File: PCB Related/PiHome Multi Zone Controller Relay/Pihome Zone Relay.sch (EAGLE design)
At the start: 17 parts, among them IC1 REG1117, M1 WIRELESS-NRF24L01, M3 ARDUINO-PRO-MINI-5.0V

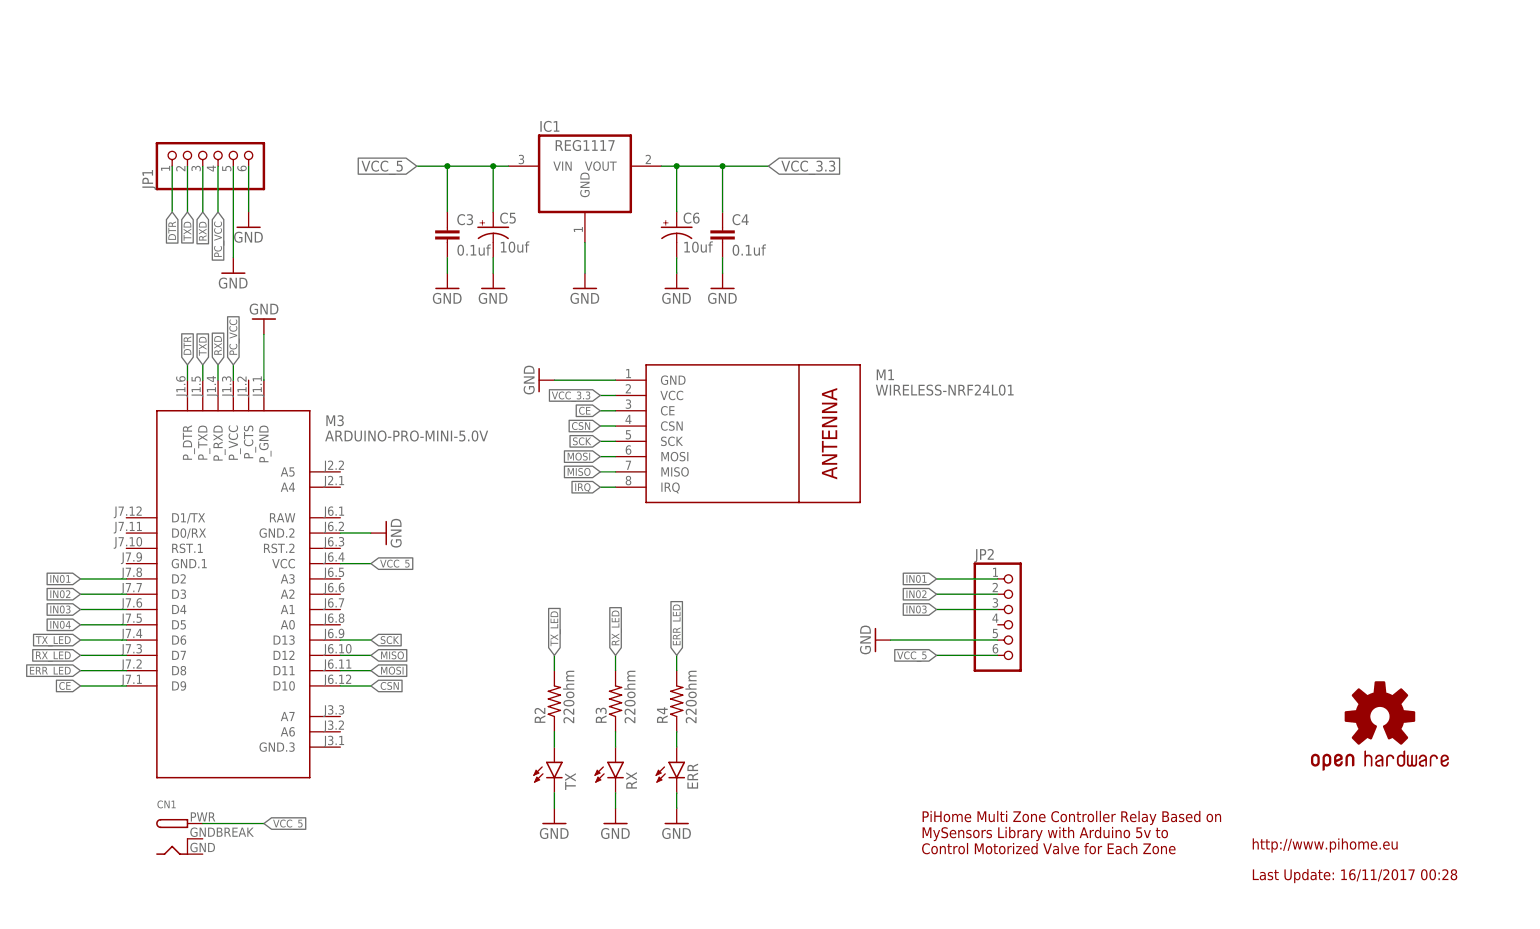
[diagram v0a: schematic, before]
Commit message: PiHome – Smart Heating Controller
PCB improvements
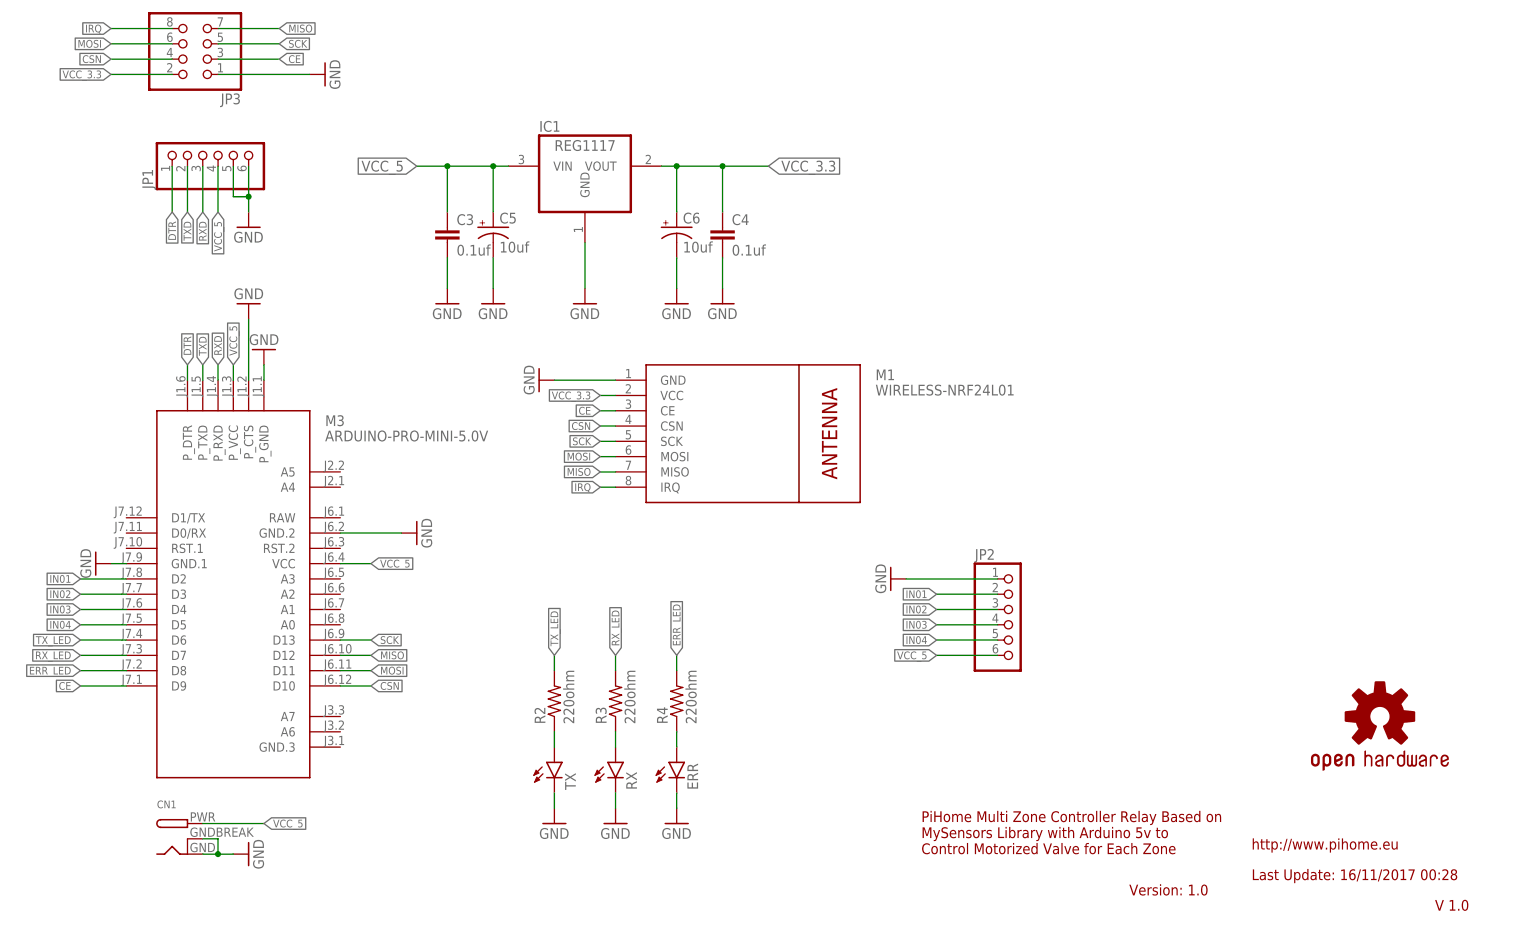
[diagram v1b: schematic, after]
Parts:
- removed LOGO1: OSHW-LOGOL, SparkFun-Aesthetics:OSHW-LOGOL
- added JP3: (no value), adafruit:PINHD-2X4
- added LOGO4: OSHW-LOGOM, SparkFun-Aesthetics:OSHW-LOGOM
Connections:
- removed net GND-: C3.2, C4.2, C5.-, C6.-, IC1.GND, JP1.5, JP1.6, M3.GND.2
- removed net PC_VCC: JP1.4, M3.P_VCC
- net CE: now also JP3.3
- net CSN: now also JP3.4
- net GND: now also C3.2, C4.2, C5.-, C6.-, CN1.GND, CN1.GNDBREAK, IC1.GND, JP1.5, JP1.6, JP2.1, JP3.1, M3.GND.1, M3.GND.2, M3.P_CTS; no longer JP2.5
- net IN01: now also JP2.2; no longer JP2.1
- net IN02: now also JP2.3; no longer JP2.2
- net IN03: now also JP2.4; no longer JP2.3
- net IN04: now also JP2.5
- net IRQ: now also JP3.8
- net MISO: now also JP3.7
- net MOSI: now also JP3.6
- net SCK: now also JP3.5
- net VCC_3.3: now also JP3.2
- net VCC_5: now also JP1.4, M3.P_VCC
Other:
- note added: "V 1.0"
- note added: "Version: 1.0"

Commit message: Improved PCB Design
Improved PCB Design
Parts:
- removed JP1: (no value), adafruit:PINHD-1X6
- removed M3: ARDUINO-PRO-MINI-5.0V, diy-modules:ARDUINO-PRO-MINI-5.0V
- added C1: 10uf, SparkFun-Capacitors:10UF-25V-20%(PTH)KIT
- added U$1: NANO, Arduino Pro Mini-Nano:NANO
- added U$2: MICRO-USB, microusb:MICRO-USB
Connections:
- removed net DTR: JP1.1, M3.P_DTR
- removed net IN01: JP2.2, M3.D2
- removed net IN02: JP2.3, M3.D3
- removed net IN03: JP2.4, M3.D4
- removed net IN04: JP2.5, M3.D5
- removed net RXD: JP1.3, M3.P_RXD
- removed net TXD: JP1.2, M3.P_TXD
- new net ZONE_01: JP2.2, U$1.D2
- new net ZONE_02: JP2.3, U$1.D3
- new net ZONE_03: JP2.4, U$1.D4
- new net ZONE_04: JP2.5, U$1.D5
- net CE: now also U$1.D9; no longer M3.D9
- net CSN: now also U$1.D10; no longer M3.D10
- net ERR_LED: now also U$1.D8; no longer M3.D8
- net GND: now also C1.-, U$1.GND, U$1.GND2, U$2.GND; no longer JP1.5, JP1.6, M3.GND.1, M3.GND.2, M3.P_CTS, M3.P_GND
- net MISO: now also U$1.D12; no longer M3.D12
- net MOSI: now also U$1.D11; no longer M3.D11
- net RX_LED: now also U$1.D7; no longer M3.D7
- net SCK: now also U$1.D13; no longer M3.D13
- net TX_LED: now also U$1.D6; no longer M3.D6
- net VCC_3.3: now also C1.+
- net VCC_5: now also U$1.5.5V, U$2.VCC; no longer JP1.4, M3.P_VCC, M3.VCC
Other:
- moved on the sheet: JP2
